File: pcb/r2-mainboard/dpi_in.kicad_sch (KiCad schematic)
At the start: 2 parts, among them J501 BTH-060-01-L-D-A-K-TR, J502 BTH-060-01-L-D-A-K-TR

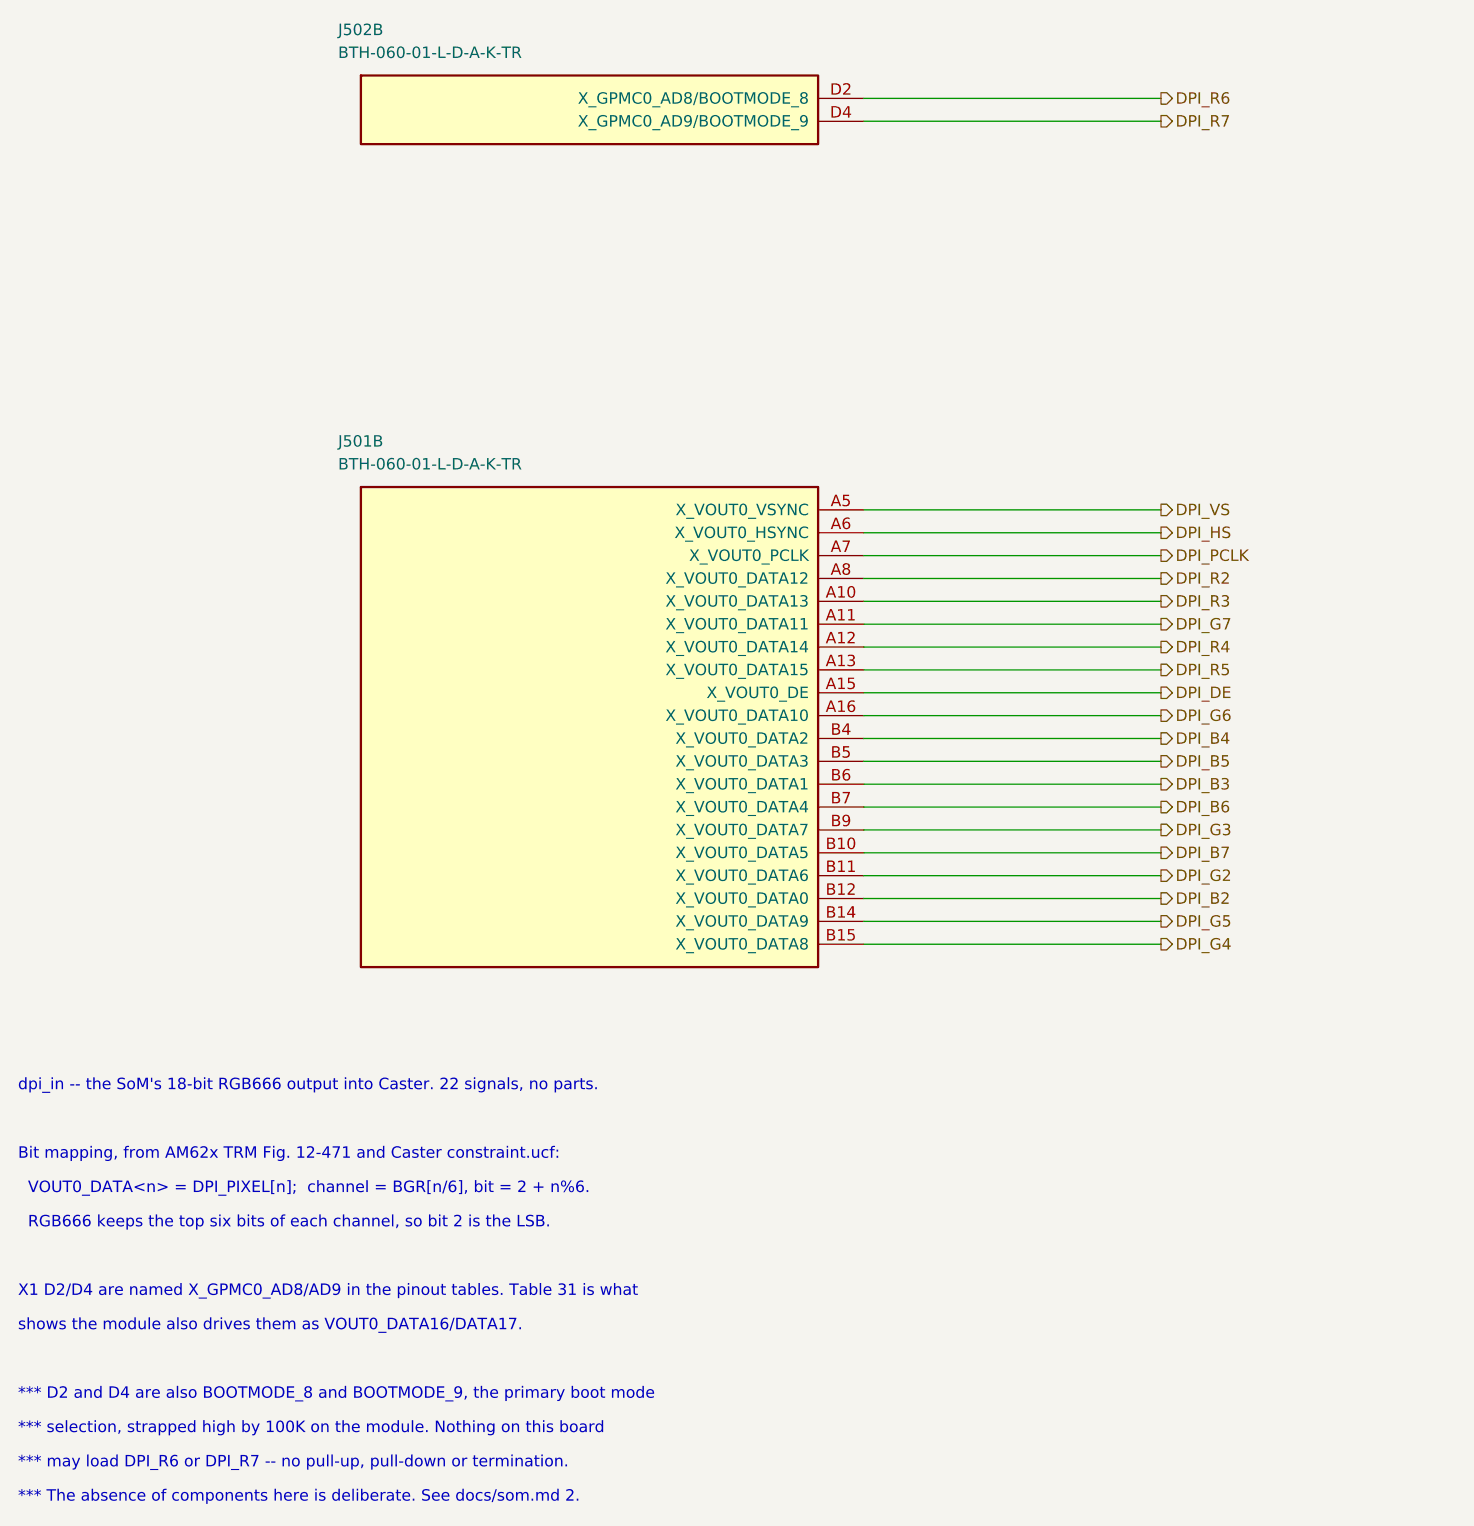
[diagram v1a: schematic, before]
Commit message: Schematics update for new chip.
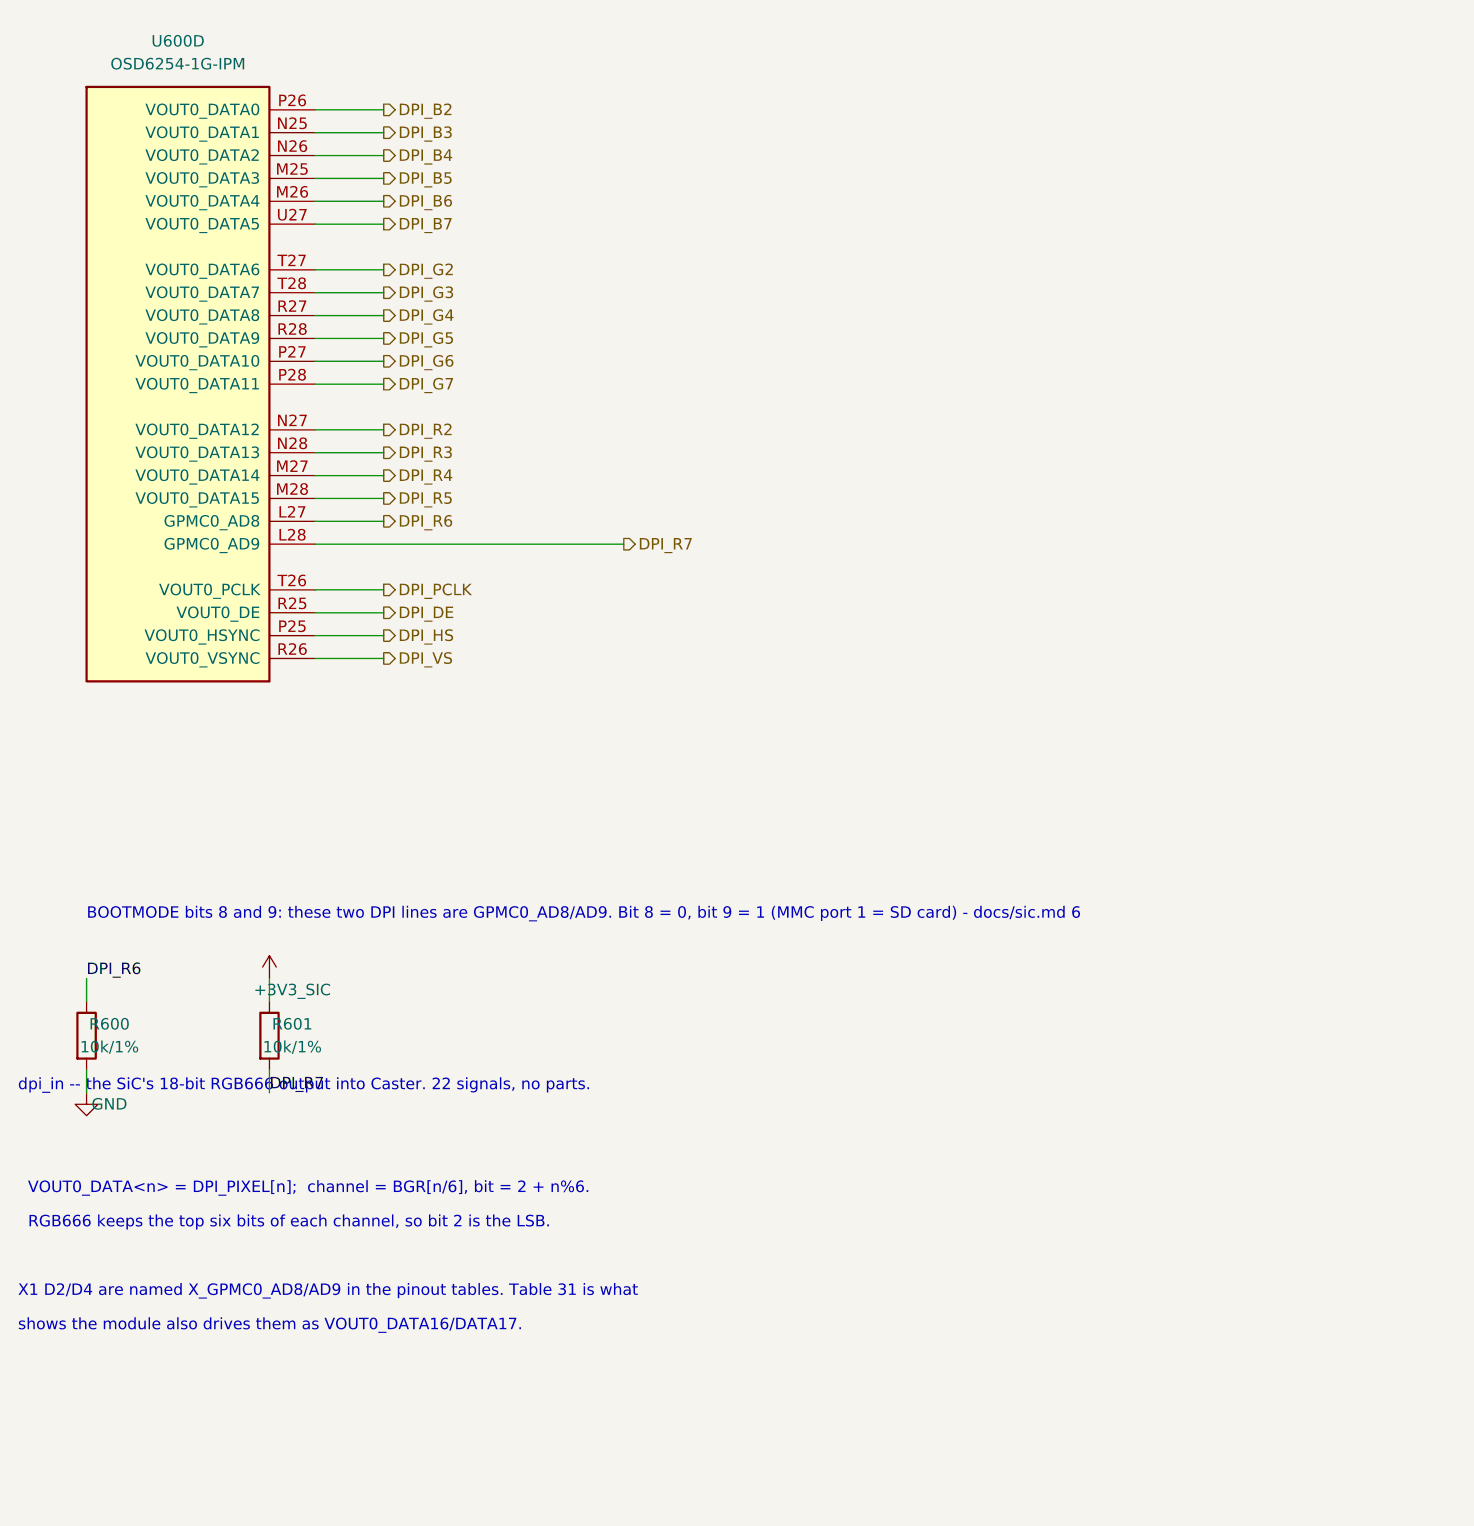
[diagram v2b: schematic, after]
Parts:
- removed J501: BTH-060-01-L-D-A-K-TR, r2:BTH-060-01-L-D-A-K_AB, symbol r2:BTH-060_AB
- removed J502: BTH-060-01-L-D-A-K-TR, r2:BTH-060-01-L-D-A-K_CD, symbol r2:BTH-060_CD
- added R600, R601: 10k/1%, Resistor_SMD:R_0402_1005Metric, symbol Device:R
- added U600: OSD6254-1G-IPM, Reflow:BGA500C50P28X18_1400X900X130, symbol Reflow:OSD6254-1G-IPM
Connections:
- net DPI_B2: now also U600.P26 (VOUT0_DATA0)
- net DPI_B3: now also U600.N25 (VOUT0_DATA1)
- net DPI_B4: now also U600.N26 (VOUT0_DATA2)
- net DPI_B5: now also U600.M25 (VOUT0_DATA3)
- net DPI_B6: now also U600.M26 (VOUT0_DATA4)
- net DPI_B7: now also U600.U27 (VOUT0_DATA5)
- net DPI_DE: now also U600.R25 (VOUT0_DE)
- net DPI_G2: now also U600.T27 (VOUT0_DATA6)
- net DPI_G3: now also U600.T28 (VOUT0_DATA7)
- net DPI_G4: now also U600.R27 (VOUT0_DATA8)
- net DPI_G5: now also U600.R28 (VOUT0_DATA9)
- net DPI_G6: now also U600.P27 (VOUT0_DATA10)
- net DPI_G7: now also U600.P28 (VOUT0_DATA11)
- net DPI_HS: now also U600.P25 (VOUT0_HSYNC)
- net DPI_PCLK: now also U600.T26 (VOUT0_PCLK)
- net DPI_R2: now also U600.N27 (VOUT0_DATA12)
- net DPI_R3: now also U600.N28 (VOUT0_DATA13)
- net DPI_R4: now also U600.M27 (VOUT0_DATA14)
- net DPI_R5: now also U600.M28 (VOUT0_DATA15)
- net DPI_R6: now also R600.1, U600.L27 (GPMC0_AD8)
- net DPI_R7: now also R601.2, U600.L28 (GPMC0_AD9)
- net DPI_VS: now also U600.R26 (VOUT0_VSYNC)
- new net +3V3_SIC: R601.1
- new net GND: R600.2
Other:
- note added: "BOOTMODE bits 8 and 9: these two DPI lines are GPMC0_AD8/AD9. Bit 8 = 0, bit 9 = 1 (MMC port 1 = SD card) - docs/sic.md 6"
- note added: "dpi_in -- the SiC's 18-bit RGB666 output into Caster. 22 signals, no parts."
- note removed: "*** D2 and D4 are also BOOTMODE_8 and BOOTMODE_9, the primary boot mode"
- note removed: "*** The absence of components here is deliberate. See docs/som.md 2."
- note removed: "*** may load DPI_R6 or DPI_R7 -- no pull-up, pull-down or termination."
- note removed: "*** selection, strapped high by 100K on the module. Nothing on this board"
- note removed: "Bit mapping, from AM62x TRM Fig. 12-471 and Caster constraint.ucf:"
- note removed: "dpi_in -- the SoM's 18-bit RGB666 output into Caster. 22 signals, no parts."
